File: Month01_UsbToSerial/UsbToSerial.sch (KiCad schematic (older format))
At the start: 14 parts, among them J1 USB_B_Micro, J2 Conn1, J3 Conn2, U1 FT232RL

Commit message: added files from mistaken working copy in separate folder
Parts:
- removed J2: Conn1, Connector_PinHeader_2.54mm:PinHeader_1x05_P2.54mm_Vertical, symbol Connector_Generic:Conn_01x05
- removed J3: Conn2, Connector_PinHeader_2.54mm:PinHeader_1x05_P2.54mm_Vertical, symbol Connector_Generic:Conn_01x05
- added J2, J3: Conn_01x07_Female, Connector_PinHeader_2.54mm:PinHeader_1x07_P2.54mm_Vertical, symbol Connector:Conn_01x07_Female
- C2: footprint Capacitor_SMD:C_0201_0603Metric -> Capacitor_SMD:C_0603_1608Metric
- JP1: footprint Jumper:SolderJumper-3_P1.3mm_Open_Pad1.0x1.5mm -> Connector_PinHeader_2.54mm:PinHeader_1x03_P2.54mm_Vertical
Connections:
- net +5V: no longer U1.19 (~RESET~)
- net CTS: now also J3.1 (Pin_1)
- net DCD: now also J3.2 (Pin_2)
- net DCR: now also J3.3 (Pin_3)
- net DTR: now also J2.6 (Pin_6)
- net GNDREF: now also J2.1 (Pin_1), J2.3 (Pin_3)
- net PWR: now also U1.19 (~RESET~), J2.2 (Pin_2)
- net RI: now also J3.4 (Pin_4)
- net RTS: now also J2.5 (Pin_5)
- net RXI: now also J3.5 (Pin_5)
- net TX0: now also J2.7 (Pin_7)
- no-connect marks 5 -> 6
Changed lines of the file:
@@
 F 0 "JP1" H 6750 2355 50  0000 C CNN
 F 1 "PowerSelect" H 6750 2264 50  0000 C CNN
-F 2 "Jumper:SolderJumper-3_P1.3mm_Open_Pad1.0x1.5mm" H 6750 2150 50  0001 C CNN
+F 2 "Connector_PinHeader_2.54mm:PinHeader_1x03_P2.54mm_Vertical" H 6750 2150 50  0001 C CNN
 F 3 "~" H 6750 2150 50  0001 C CNN
 	1    6750 2150
@@
 Wire Wire Line
 	7350 5700 7100 5700
-$Comp
-L power:+5V #PWR0104
-U 1 1 5D1D3707
-P 4450 3750
-F 0 "#PWR0104" H 4450 3600 50  0001 C CNN
-F 1 "+5V" H 4465 3923 50  0000 C CNN
-F 2 "" H 4450 3750 50  0001 C CNN
-F 3 "" H 4450 3750 50  0001 C CNN
-	1    4450 3750
-	1    0    0    -1
-$EndComp
-Wire Wire Line
-	4900 3800 4450 3800
-Wire Wire Line
-	4450 3800 4450 3750
 Wire Wire Line
 	5500 5000 5600 5000
@@
 F 0 "C2" H 2792 2746 50  0000 L CNN
 F 1 "100nF" H 2792 2655 50  0000 L CNN
-F 2 "Capacitor_SMD:C_0201_0603Metric" H 2700 2700 50  0001 C CNN
+F 2 "Capacitor_SMD:C_0603_1608Metric" H 2700 2700 50  0001 C CNN
 F 3 "~" H 2700 2700 50  0001 C CNN
 	1    2700 2700
@@
 Wire Wire Line
 	6800 3300 6500 3300
-$Comp
-L Connector_Generic:Conn_01x05 J2
-U 1 1 5D21C07B
-P 9250 2950
-F 0 "J2" H 9330 2992 50  0000 L CNN
-F 1 "Conn1" H 9330 2901 50  0000 L CNN
-F 2 "Connector_PinHeader_2.54mm:PinHeader_1x05_P2.54mm_Vertical" H 9250 2950 50  0001 C CNN
-F 3 "~" H 9250 2950 50  0001 C CNN
-	1    9250 2950
-	1    0    0    -1
-$EndComp
-$Comp
-L Connector_Generic:Conn_01x05 J3
-U 1 1 5D21C0F8
-P 9250 3600
-F 0 "J3" H 9330 3642 50  0000 L CNN
-F 1 "Conn2" H 9330 3551 50  0000 L CNN
-F 2 "Connector_PinHeader_2.54mm:PinHeader_1x05_P2.54mm_Vertical" H 9250 3600 50  0001 C CNN
-F 3 "~" H 9250 3600 50  0001 C CNN
-	1    9250 3600
-	1    0    0    -1
-$EndComp
+Text GLabel 8700 3350 0    50   Output ~ 0
+TX0
+Text GLabel 8700 4750 0    50   Output ~ 0
+RXI
 Text GLabel 8700 3150 0    50   Output ~ 0
-TX0
-Text GLabel 8700 2750 0    50   Output ~ 0
-RXI
-Text GLabel 8700 2950 0    50   Output ~ 0
 RTS
-Text GLabel 8700 3400 0    50   Output ~ 0
+Text GLabel 8700 4350 0    50   Output ~ 0
 CTS
-Text GLabel 8700 3050 0    50   Output ~ 0
+Text GLabel 8700 3250 0    50   Output ~ 0
 DTR
-Text GLabel 8700 3600 0    50   Output ~ 0
+Text GLabel 8700 4550 0    50   Output ~ 0
 DCR
-Text GLabel 8700 3500 0    50   Output ~ 0
+Text GLabel 8700 4450 0    50   Output ~ 0
 DCD
-Text GLabel 8700 3800 0    50   Output ~ 0
+Text GLabel 8700 4650 0    50   Output ~ 0
 RI
 Text GLabel 8700 2850 0    50   Output ~ 0
@@
 L power:GNDREF #PWR0109
 U 1 1 5D228737
-P 8350 3900
-F 0 "#PWR0109" H 8350 3650 50  0001 C CNN
-F 1 "GNDREF" H 8355 3727 50  0000 C CNN
-F 2 "" H 8350 3900 50  0001 C CNN
-F 3 "" H 8350 3900 50  0001 C CNN
-	1    8350 3900
-	1    0    0    -1
-$EndComp
-Wire Wire Line
-	9050 3400 8700 3400
-Wire Wire Line
-	8700 3500 9050 3500
-Wire Wire Line
-	9050 3600 8700 3600
-Wire Wire Line
-	9050 3700 8350 3700
-Wire Wire Line
-	8350 3700 8350 3900
-Wire Wire Line
-	8700 3800 9050 3800
-Wire Wire Line
-	8700 2750 9050 2750
+P 8300 2800
+F 0 "#PWR0109" H 8300 2550 50  0001 C CNN
+F 1 "GNDREF" H 8305 2627 50  0000 C CNN
+F 2 "" H 8300 2800 50  0001 C CNN
+F 3 "" H 8300 2800 50  0001 C CNN
+	1    8300 2800
+	1    0    0    -1
+$EndComp
+Wire Wire Line
+	9050 4350 8700 4350
+Wire Wire Line
+	8700 4450 9050 4450
+Wire Wire Line
+	9050 4550 8700 4550
+Wire Wire Line
+	7100 2150 6950 2150
+Wire Wire Line
+	6550 2150 6400 2150
+Text GLabel 4200 3800 0    50   Input ~ 0
+PWR
+Wire Wire Line
+	4900 3800 4200 3800
+Wire Wire Line
+	9050 4650 8700 4650
+Wire Wire Line
+	8700 4750 9050 4750
+Wire Wire Line
+	8700 3150 9050 3150
+Wire Wire Line
+	9050 3250 8700 3250
+Wire Wire Line
+	8700 3350 9050 3350
 Wire Wire Line
 	9050 2850 8700 2850
 Wire Wire Line
-	8700 2950 9050 2950
-Wire Wire Line
-	9050 3050 8700 3050
-Wire Wire Line
-	8700 3150 9050 3150
-Wire Wire Line
-	7100 2150 6950 2150
-Wire Wire Line
-	6550 2150 6400 2150
+	9050 2750 8450 2750
+Wire Wire Line
+	8300 2750 8300 2800
+$Comp
+L Connector:Conn_01x07_Female J3
+U 1 1 5D288061
+P 9250 4650
+F 0 "J3" H 9277 4676 50  0000 L CNN
+F 1 "Conn_01x07_Female" H 9277 4585 50  0000 L CNN
+F 2 "Connector_PinHeader_2.54mm:PinHeader_1x07_P2.54mm_Vertical" H 9250 4650 50  0001 C CNN
+F 3 "~" H 9250 4650 50  0001 C CNN
+	1    9250 4650
+	1    0    0    -1
+$EndComp
+$Comp
+L Connector:Conn_01x07_Female J2
+U 1 1 5D28816E
+P 9250 3050
+F 0 "J2" H 9277 3076 50  0000 L CNN
+F 1 "Conn_01x07_Female" H 9277 2985 50  0000 L CNN
+F 2 "Connector_PinHeader_2.54mm:PinHeader_1x07_P2.54mm_Vertical" H 9250 3050 50  0001 C CNN
+F 3 "~" H 9250 3050 50  0001 C CNN
+	1    9250 3050
+	1    0    0    -1
+$EndComp
+Wire Wire Line
+	9050 2950 8450 2950
+Wire Wire Line
+	8450 2950 8450 2750
+Connection ~ 8450 2750
+Wire Wire Line
+	8450 2750 8300 2750
+NoConn ~ 2450 3600
 $EndSCHEMATC

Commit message: added extra text to the bottom layer of the board, changed pin headers to 8 instead of 7
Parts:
- J2, J3: value Conn_01x07_Female -> Conn_01x08_Male; footprint Connector_PinHeader_2.54mm:PinHeader_1x07_P2.54mm_Vertical -> Connector_PinHeader_2.54mm:PinHeader_1x08_P2.54mm_Vertical; symbol Connector:Conn_01x07_Female -> Connector:Conn_01x08_Male
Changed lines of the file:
@@
 	8300 2750 8300 2800
 $Comp
-L Connector:Conn_01x07_Female J3
+L Connector:Conn_01x08_Male J3
 U 1 1 5D288061
 P 9250 4650
 F 0 "J3" H 9277 4676 50  0000 L CNN
-F 1 "Conn_01x07_Female" H 9277 4585 50  0000 L CNN
-F 2 "Connector_PinHeader_2.54mm:PinHeader_1x07_P2.54mm_Vertical" H 9250 4650 50  0001 C CNN
+F 1 "Conn_01x08_Male" H 9277 4585 50  0000 L CNN
+F 2 "Connector_PinHeader_2.54mm:PinHeader_1x08_P2.54mm_Vertical" H 9250 4650 50  0001 C CNN
 F 3 "~" H 9250 4650 50  0001 C CNN
 	1    9250 4650
-	1    0    0    -1
+	-1   0    0    -1
 $EndComp
 $Comp
-L Connector:Conn_01x07_Female J2
+L Connector:Conn_01x08_Male J2
 U 1 1 5D28816E
 P 9250 3050
 F 0 "J2" H 9277 3076 50  0000 L CNN
-F 1 "Conn_01x07_Female" H 9277 2985 50  0000 L CNN
-F 2 "Connector_PinHeader_2.54mm:PinHeader_1x07_P2.54mm_Vertical" H 9250 3050 50  0001 C CNN
+F 1 "Conn_01x08_Male" H 9277 2985 50  0000 L CNN
+F 2 "Connector_PinHeader_2.54mm:PinHeader_1x08_P2.54mm_Vertical" H 9250 3050 50  0001 C CNN
 F 3 "~" H 9250 3050 50  0001 C CNN
 	1    9250 3050
-	1    0    0    -1
+	-1   0    0    -1
 $EndComp
 Wire Wire Line

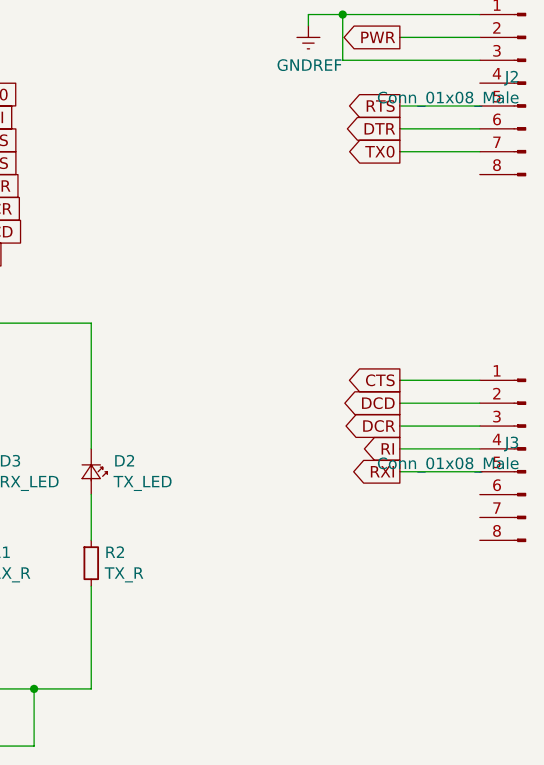
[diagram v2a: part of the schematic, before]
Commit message: Minor modification to the board and schematic to utilise unused pins, deleted old files
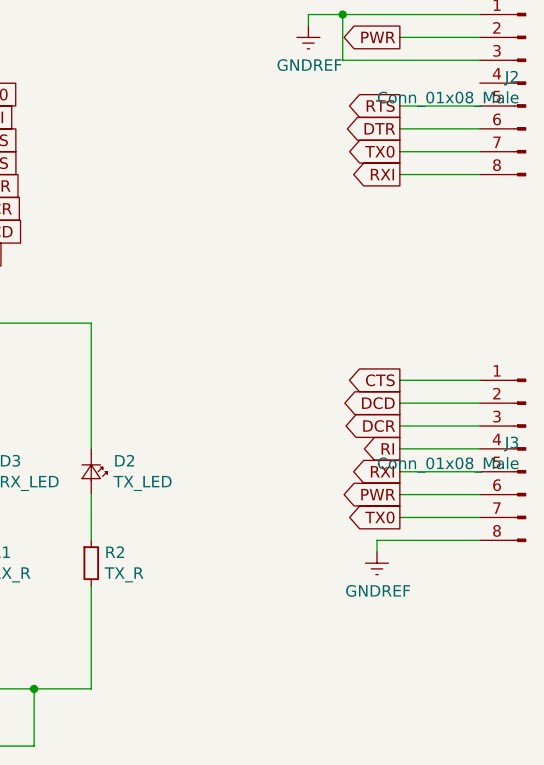
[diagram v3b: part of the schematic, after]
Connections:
- net GNDREF: now also J3.8 (Pin_8)
- net PWR: now also J3.6 (Pin_6)
- net RXI: now also J2.8 (Pin_8)
- net TX0: now also J3.7 (Pin_7)
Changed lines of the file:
@@
 encoding utf-8
 Sheet 1 1
-Title ""
-Date ""
-Rev ""
-Comp ""
-Comment1 ""
+Title "UsbToSerial"
+Date "2019-07-27"
+Rev "V.0.1"
+Comp "-"
+Comment1 "Author: Richard Clubb"
 Comment2 ""
 Comment3 ""
@@
 	8450 2750 8300 2750
 NoConn ~ 2450 3600
+$Comp
+L power:GNDREF #PWR0104
+U 1 1 5D3C4B10
+P 8600 5100
+F 0 "#PWR0104" H 8600 4850 50  0001 C CNN
+F 1 "GNDREF" H 8605 4927 50  0000 C CNN
+F 2 "" H 8600 5100 50  0001 C CNN
+F 3 "" H 8600 5100 50  0001 C CNN
+	1    8600 5100
+	1    0    0    -1
+$EndComp
+Wire Wire Line
+	9050 5050 8600 5050
+Wire Wire Line
+	8600 5050 8600 5100
+Text GLabel 8700 4850 0    50   Output ~ 0
+PWR
+Wire Wire Line
+	9050 4850 8700 4850
+Text GLabel 8700 4950 0    50   Output ~ 0
+TX0
+Wire Wire Line
+	9050 4950 8700 4950
+Text GLabel 8700 3450 0    50   Output ~ 0
+RXI
+Wire Wire Line
+	8700 3450 9050 3450
 $EndSCHEMATC

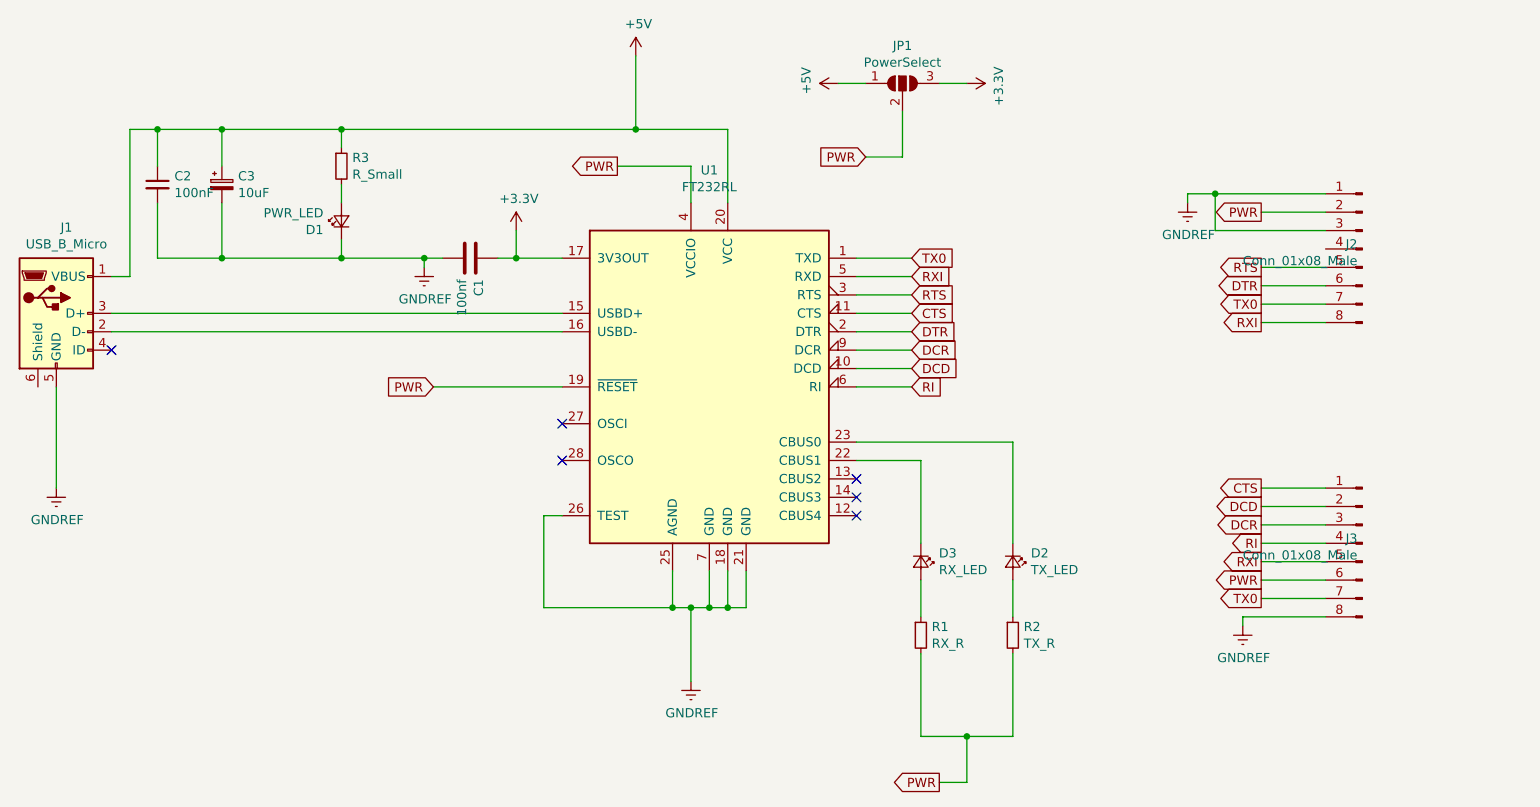
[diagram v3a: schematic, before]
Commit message: #3 added via and track to back of board for DTR pin
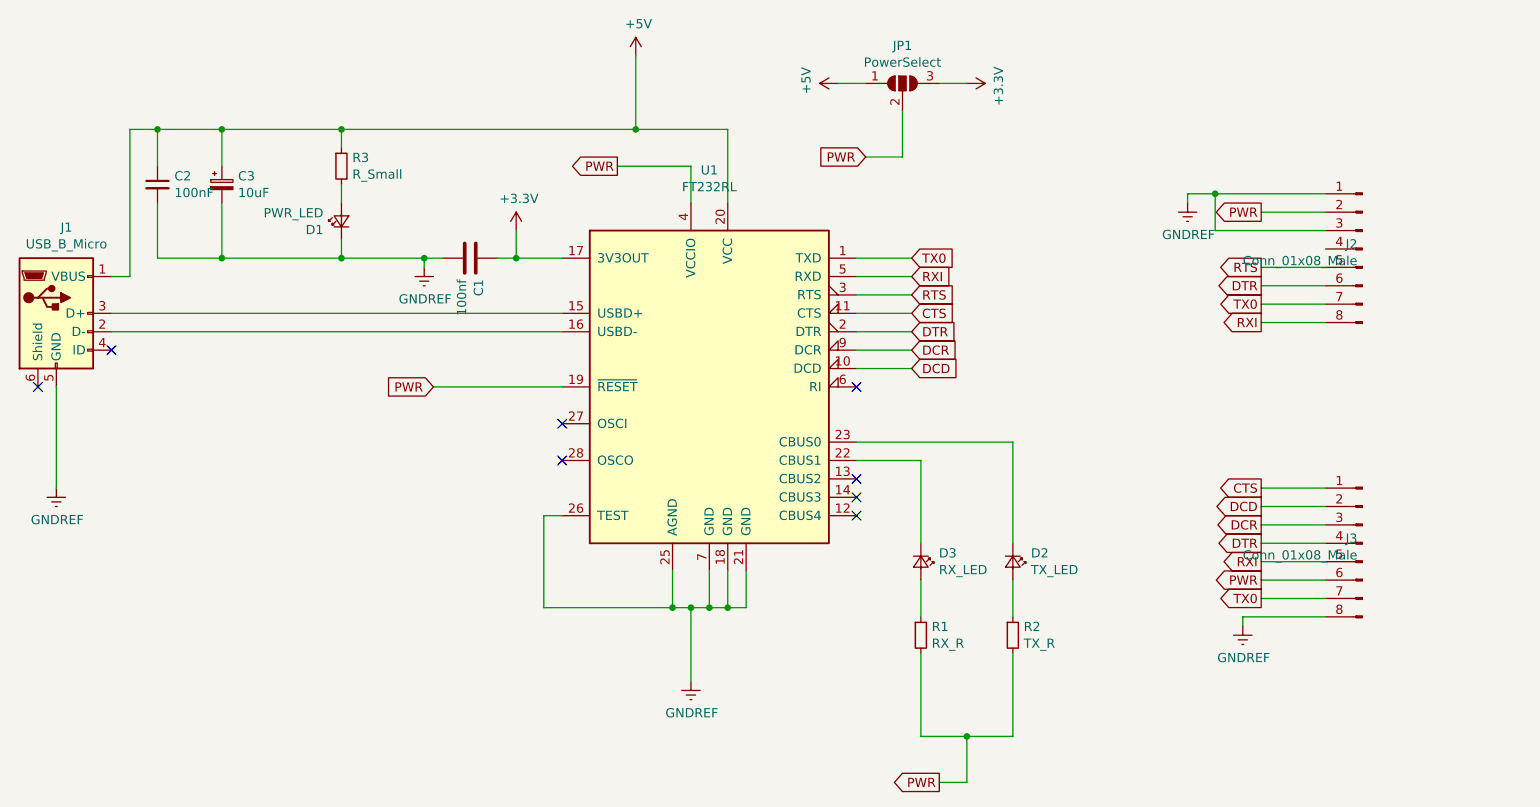
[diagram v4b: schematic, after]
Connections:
- net DTR: now also J3.4 (Pin_4)
- net RI: no longer names the net of U1.6 (RI)
- net RI: no longer J3.4 (Pin_4)
- no-connect marks 6 -> 8
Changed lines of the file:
@@
 Text GLabel 6800 3600 2    50   Input ~ 0
 DCR
-Text GLabel 6800 3800 2    50   Input ~ 0
-RI
-Wire Wire Line
-	6800 3800 6500 3800
 Wire Wire Line
 	6500 3700 6800 3700
@@
 Text GLabel 8700 4450 0    50   Output ~ 0
 DCD
-Text GLabel 8700 4650 0    50   Output ~ 0
-RI
 Text GLabel 8700 2850 0    50   Output ~ 0
 PWR
@@
 Wire Wire Line
 	8700 3450 9050 3450
+NoConn ~ 6500 3800
+NoConn ~ 2050 3800
+Text GLabel 8700 4650 0    50   Output ~ 0
+DTR
 $EndSCHEMATC
